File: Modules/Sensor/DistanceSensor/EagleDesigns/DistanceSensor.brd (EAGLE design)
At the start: 100 x 80 mm, 10 parts, among them U1 TINY85-20-DIP

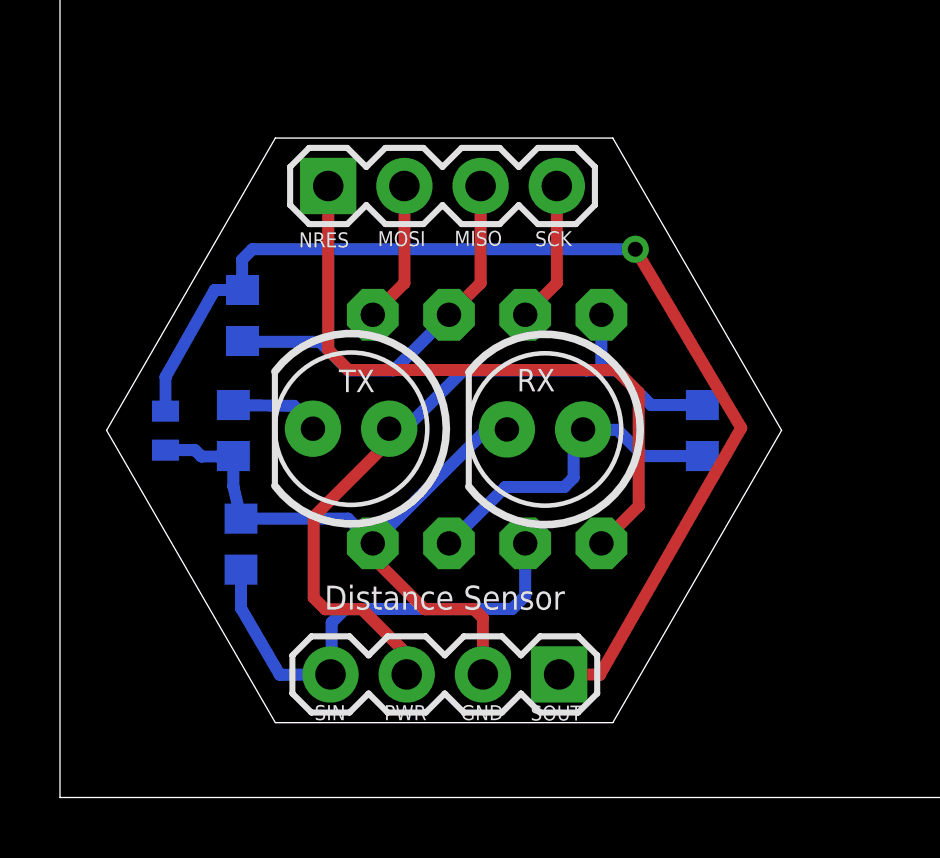
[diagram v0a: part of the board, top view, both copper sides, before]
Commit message: DistanceSensor: added another IR-TX LED #9
to increase the range of the module.
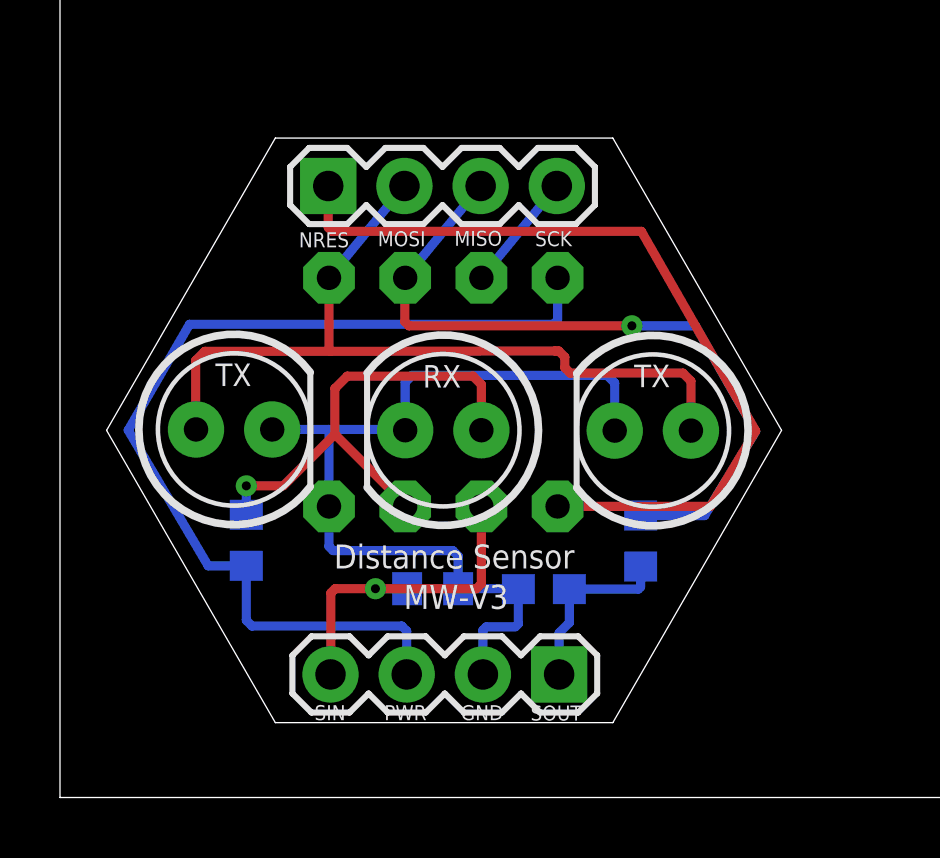
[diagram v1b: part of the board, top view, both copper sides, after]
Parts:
- removed R2: 30, adafruit:R0603
- removed TX-IR: (no value), SparkFun-LED:LED5MM
- added TX-IR1, TX-IR2: (no value), SparkFun-LED:LED5MM
- C1: device adafruit:C0402 -> adafruit:C0603
- R3: value 1M -> 100K
- moved R3 15.6 mm to (6.21, 8.57), turned to 270 degrees
- moved R4 15.3 mm to (19.4, 8.55), turned to 90 degrees
- moved C1 13.7 mm to (16.1, 6.95), turned to 0 degrees
- moved R1 6.56 mm to (12.4, 6.96), turned to 0 degrees
- moved RX-IR 3.39 mm to (12.8, 12.2)
- moved U1 1.91 mm to (12.8, 13.5)
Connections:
- net SENSOR renamed IR-RX
- removed net MOSI: JP2.2, U1.5
- removed net N$2: R2.2, TX-IR.K
- new net IR-TX(MOSI): JP2.2, TX-IR1.A, TX-IR2.A, U1.5
- net 1X3SOUT: now also C1.1; no longer C1.2
- net GND: now also C1.2, TX-IR1.K, TX-IR2.K; no longer C1.1, R2.1
- net VCC: no longer TX-IR.A
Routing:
- net 1X3SOUT: track 37.4 -> 6.07 mm, vias 1 -> 0
- net IR-TX(MOSI): track 0.00 -> 27.6 mm
- net OUT(MISO): track 12.8 -> 24.6 mm, vias 0 -> 1
- net VCC: track 25.0 -> 33.1 mm
- net GND: track 22.7 -> 30.2 mm
- net NRES: track 21.9 -> 27.6 mm
- net MOSI: track 4.73 -> 0.00 mm
- net IR-RX: track 11.8 -> 16.2 mm, vias 0 -> 1
- net 1X3SIN: track 15.9 -> 11.5 mm, vias 0 -> 1
- net N$2: track 3.01 -> 0.00 mm
- net SCK: track 4.73 -> 3.96 mm
